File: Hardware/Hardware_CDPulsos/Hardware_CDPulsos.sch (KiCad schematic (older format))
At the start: 1 part

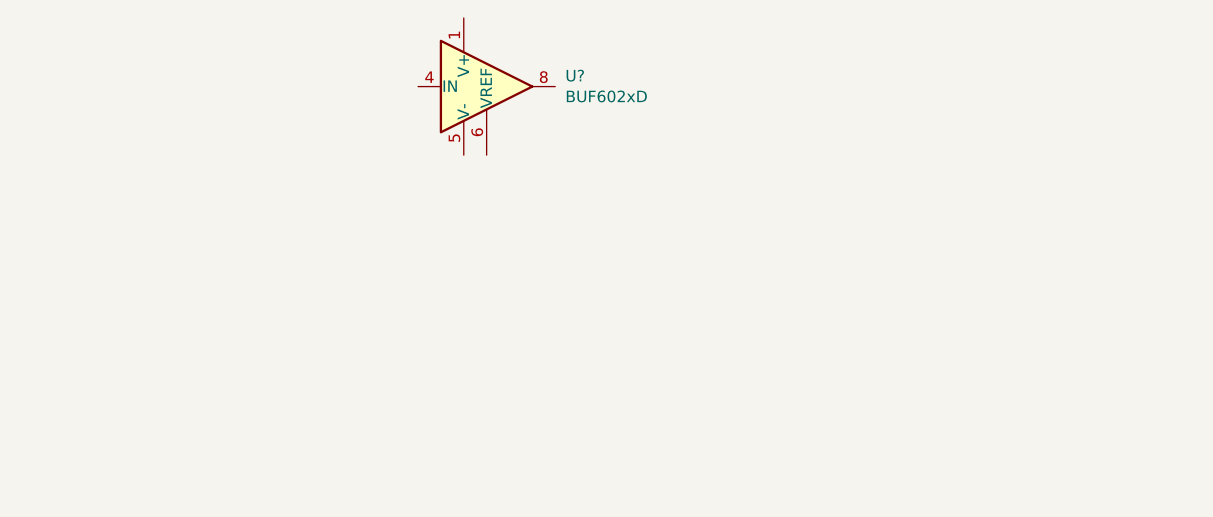
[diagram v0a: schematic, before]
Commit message: Iniciada estrutura de dados do firmware (lcd,sd_card,buttons). Iniciado esquemático do hardware
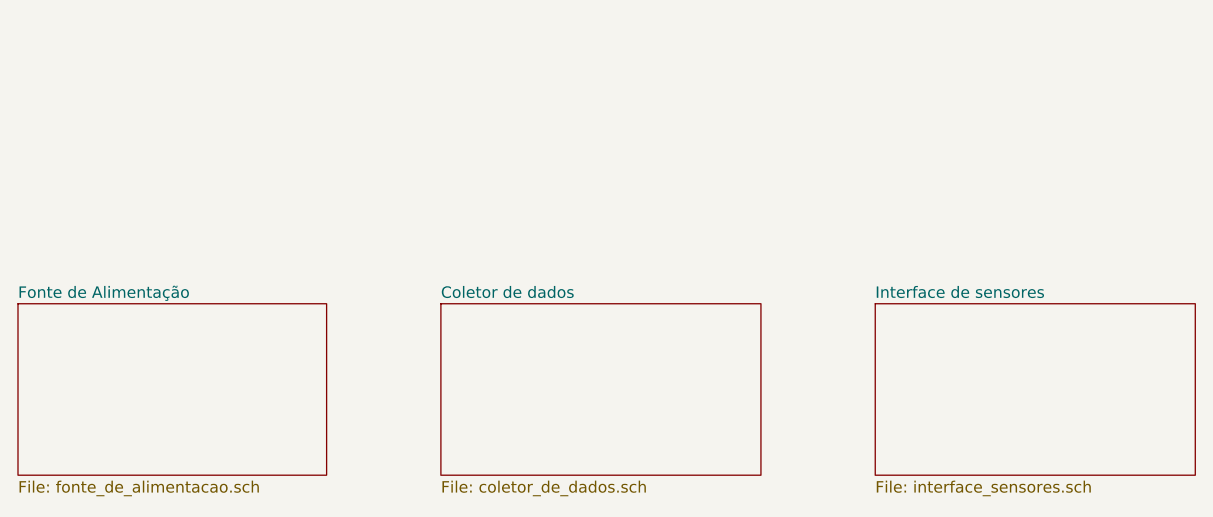
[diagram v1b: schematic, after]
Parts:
- removed U?: BUF602xD, Package_SO:SOIC-8_3.9x4.9mm_P1.27mm, symbol Amplifier_Buffer:BUF602xD
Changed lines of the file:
@@
 $Descr A4 11693 8268
 encoding utf-8
-Sheet 1 1
+Sheet 1 4
 Title ""
 Date ""
@@
 Comment4 ""
 $EndDescr
-$Comp
-L Amplifier_Buffer:BUF602xD U?
-U 1 1 60F8900D
-P 4000 2550
-F 0 "U?" H 4344 2596 50  0000 L CNN
-F 1 "BUF602xD" H 4344 2505 50  0000 L CNN
-F 2 "Package_SO:SOIC-8_3.9x4.9mm_P1.27mm" H 4000 2250 50  0001 C CNN
-F 3 "http://www.ti.com/lit/ds/symlink/buf602.pdf" H 4000 2550 50  0001 C CNN
-	1    4000 2550
-	1    0    0    -1
-$EndComp
+$Sheet
+S 3800 3500 1400 750
+U 60FDA959
+F0 "Coletor de dados" 50
+F1 "coletor_de_dados.sch" 50
+$EndSheet
+$Sheet
+S 5700 3500 1400 750
+U 60FDA9B2
+F0 "Interface de sensores" 50
+F1 "interface_sensores.sch" 50
+$EndSheet
+$Sheet
+S 1950 3500 1350 750
+U 60FE00C8
+F0 "Fonte de Alimentação" 50
+F1 "fonte_de_alimentacao.sch" 50
+$EndSheet
 $EndSCHEMATC
